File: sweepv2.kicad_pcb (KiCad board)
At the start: 2 copper layers, 216.9 x 86.9 mm, 51 parts, among them J1 AudioJack4dpb, J2 AudioJack4dpb, SW10 SW_Push, SW11 SW_Push, SW11_r1 SW_Push, SW12 SW_Push, SW12_r1 SW_Push, SW13_r1 SW_Push, SW14 SW_Push, SW15 SW_Push, SW15_r1 SW_Push, SW16 SW_Push, SW16_r1 SW_Push, SW17 SW_Push, SW17_r1 SW_Push, SW18 SW_Push, SW18_r1 SW_Push, SW2 SW_Push, SW20 SW_Push, SW20_r1 SW_Push, SW21 SW_Push, SW21_r1 SW_Push, SW2_r1 SW_Push, SW3 SW_Push, SW3_r1 SW_Push, SW4 SW_Push, SW4_r1 SW_Push, SW5 SW_Push, SW5_r1 SW_Push, SW6 SW_Push, SW6_r1 SW_Push, SW7_r1 SW_Push, SW8 SW_Push, SW8_r1 SW_Push, SW9 SW_Push, SW9_r1 SW_Push, U1 ProMicro-kbd, U2 ProMicro-kbd

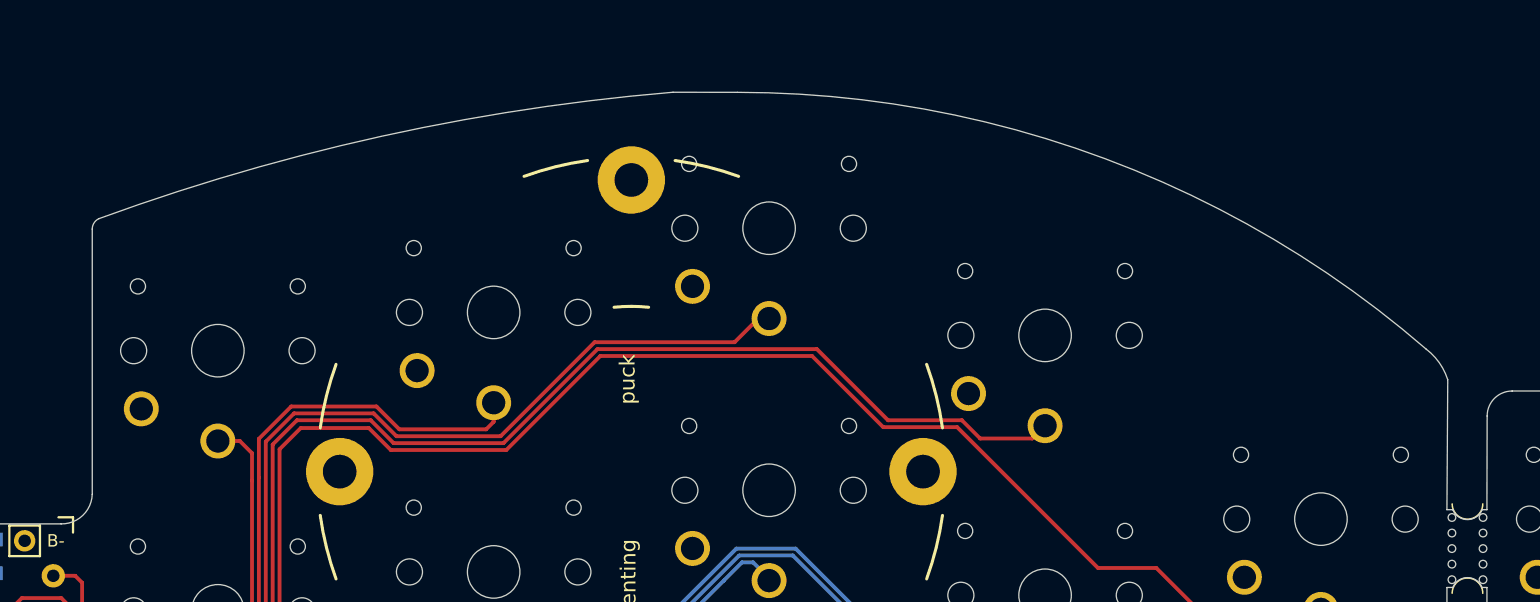
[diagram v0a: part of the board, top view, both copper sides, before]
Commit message: Copy cutout to other half
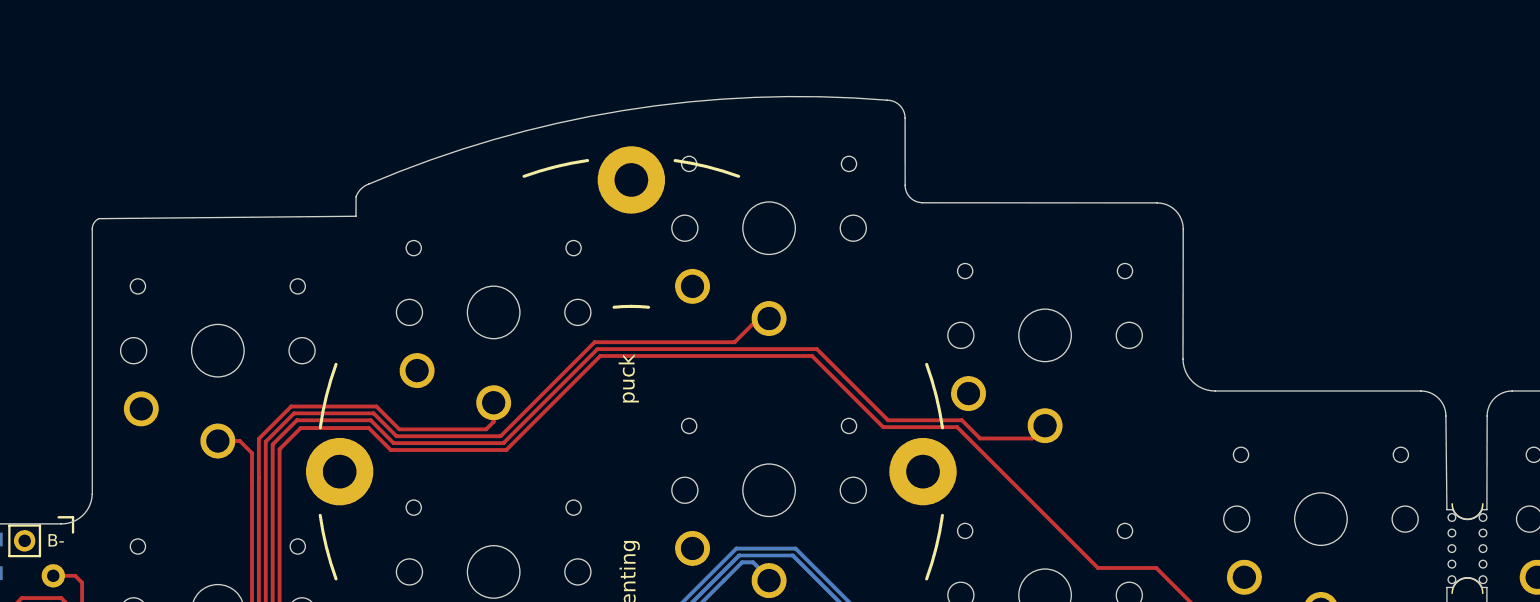
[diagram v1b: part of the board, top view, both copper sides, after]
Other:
- board size 216.9 x 86.9 mm -> 216.9 x 86.6 mm
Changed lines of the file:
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@@
   (gr_line (start 129.3495 77.724) (end 128.96 77.724) (layer "Edge.Cuts") (width 0.05))
   (gr_line (start 131.572 53.848) (end 131.572 72.644) (layer "Edge.Cuts") (width 0.05))
-  (gr_line (start 78.412223 21.502679) (end 82.613611 21.508139) (layer "Edge.Cuts") (width 0.05))
   (gr_line (start 21.792 50.442) (end 21.792 58.42) (layer "Edge.Cuts") (width 0.05))
   (gr_line (start 128.96 77.724) (end 128.975507 89.545022) (layer "Edge.Cuts") (width 0.05))
-  (gr_arc (start 127.587 38.265) (mid 128.457071 39.160882) (end 129.013945 40.278702) (layer "Edge.Cuts") (width 0.05))
   (gr_arc (start 128.975507 89.545022) (mid 128.324689 90.873432) (end 126.936 91.383119) (layer "Edge.Cuts") (width 0.05))
-  (gr_line (start 40.481999 47.763999) (end 40.481955 30.439419) (layer "Edge.Cuts") (width 0.05))
   (gr_line (start 21.792 66.548) (end 21.792 73.914) (layer "Edge.Cuts") (width 0.05))
   (gr_line (start 23.526696 88.85815) (end 34.034 107.451265) (layer "Edge.Cuts") (width 0.05))
   (gr_arc (start 40.481999 47.763999) (mid 39.859467 49.145717) (end 38.446998 49.694917) (layer "Edge.Cuts") (width 0.05))
-  (gr_arc (start 40.91671 29.758889) (mid 59.388121 24.375764) (end 78.412223 21.502679) (layer "Edge.Cuts") (width 0.05))
   (gr_arc (start 58.294866 98.863946) (mid 92.415558 93.289555) (end 126.936 91.383119) (layer "Edge.Cuts") (width 0.05))
   (gr_arc (start 23.526696 88.85815) (mid 22.237087 85.295347) (end 21.78 81.534) (layer "Edge.Cuts") (width 0.05))
@@
   (gr_line (start 38.446998 49.694917) (end 22.542 49.692) (layer "Edge.Cuts") (width 0.05))
   (gr_line (start 21.792 58.42) (end 21.792 66.548) (layer "Edge.Cuts") (width 0.05))
-  (gr_arc (start 40.481955 30.439419) (mid 40.599921 30.035645) (end 40.91671 29.758889) (layer "Edge.Cuts") (width 0.05))
   (gr_arc (start 36.766 108.05) (mid 35.275005 108.32098) (end 34.034 107.451265) (layer "Edge.Cuts") (width 0.05))
-  (gr_arc (start 82.613611 21.508139) (mid 106.610476 25.833455) (end 127.587 38.265) (layer "Edge.Cuts") (width 0.05))
   (gr_arc (start 36.766 108.05) (mid 47.217512 102.723597) (end 58.294866 98.863946) (layer "Edge.Cuts") (width 0.05))
   (gr_line (start 21.792 73.914) (end 21.78 81.534) (layer "Edge.Cuts") (width 0.05))
   (gr_line (start 128.96 53.848) (end 128.96 72.644) (layer "Edge.Cuts") (width 0.05))
-  (gr_line (start 129.013945 40.278702) (end 128.96 48.768) (layer "Edge.Cuts") (width 0.05))
+  (gr_arc (start 57.71268 28.330207) (mid 58.032549 27.821881) (end 58.540875 27.502012) (layer "Edge.Cuts") (width 0.05))
+  (gr_arc (start 58.540875 27.502012) (mid 75.136595 22.701228) (end 92.399358 22.021187) (layer "Edge.Cuts") (width 0.05))
+  (gr_line (start 93.56998 23.191809) (end 93.574586 27.576715) (layer "Edge.Cuts") (width 0.05))
+  (gr_arc (start 110.033903 28.730867) (mid 111.238908 29.229997) (end 111.738038 30.435002) (layer "Edge.Cuts") (width 0.05))
+  (gr_line (start 111.738038 30.435002) (end 111.721869 38.927938) (layer "Edge.Cuts") (width 0.05))
+  (gr_line (start 110.033903 28.730867) (end 94.708474 28.721612) (layer "Edge.Cuts") (width 0.05))
   (gr_line (start 133.216808 41.015954) (end 146.643428 41.015954) (layer "Edge.Cuts") (width 0.05))
+  (gr_line (start 113.836572 41.015954) (end 127.263192 41.015954) (layer "Edge.Cuts") (width 0.05))
   (gr_arc (start 201.939125 27.502012) (mid 202.447457 27.821875) (end 202.76732 28.330207) (layer "Edge.Cuts") (width 0.05))
   (gr_line (start 202.767321 28.330207) (end 202.770663 29.602302) (layer "Edge.Cuts") (width 0.05))
   (gr_arc (start 168.080642 22.021187) (mid 185.343405 22.701228) (end 201.939125 27.502012) (layer "Edge.Cuts") (width 0.05))
   (gr_line (start 131.572 48.768) (end 131.2545 48.768) (layer "Edge.Cuts") (width 0.05))
+  (gr_arc (start 127.263192 41.015954) (mid 128.415693 41.493335) (end 128.893074 42.645836) (layer "Edge.Cuts") (width 0.05))
+  (gr_arc (start 94.708474 28.71612) (mid 93.904741 28.38206) (end 93.574586 27.576715) (layer "Edge.Cuts") (width 0.05))
   (gr_line (start 148.758131 38.927938) (end 148.741962 30.435002) (layer "Edge.Cuts") (width 0.05))
   (gr_line (start 166.905414 27.576715) (end 166.91002 23.191809) (layer "Edge.Cuts") (width 0.05))
@@
   (gr_arc (start 131.254499 72.644) (mid 130.302 73.288873) (end 129.349501 72.643999) (layer "Edge.Cuts") (width 0.05))
   (gr_line (start 131.572 53.848) (end 131.2545 53.848) (layer "Edge.Cuts") (width 0.05))
+  (gr_arc (start 92.399358 22.021187) (mid 93.227113 22.364054) (end 93.56998 23.191809) (layer "Edge.Cuts") (width 0.05))
+  (gr_line (start 57.709337 29.602302) (end 40.91671 29.758889) (layer "Edge.Cuts") (width 0.05))
   (gr_arc (start 129.349501 77.724) (mid 130.302 77.079127) (end 131.254499 77.724001) (layer "Edge.Cuts") (width 0.05))
   (gr_arc (start 166.905414 27.576715) (mid 166.575259 28.38206) (end 165.771526 28.71612) (layer "Edge.Cuts") (width 0.05))
   (gr_arc (start 131.586926 42.645836) (mid 132.064307 41.493335) (end 133.216808 41.015954) (layer "Edge.Cuts") (width 0.05))
+  (gr_line (start 40.481955 30.439419) (end 40.481999 47.763999) (layer "Edge.Cuts") (width 0.05))
+  (gr_line (start 128.96 48.768) (end 128.893074 42.645836) (layer "Edge.Cuts") (width 0.05))
+  (gr_line (start 57.709337 29.602302) (end 57.712679 28.330207) (layer "Edge.Cuts") (width 0.05))
+  (gr_arc (start 40.481955 30.439419) (mid 40.599943 30.035659) (end 40.91671 29.758889) (layer "Edge.Cuts") (width 0.05))
   (gr_line (start 219.56329 29.758889) (end 202.770663 29.602302) (layer "Edge.Cuts") (width 0.05))
   (gr_arc (start 166.91002 23.191809) (mid 167.252887 22.364054) (end 168.080642 22.021187) (layer "Edge.Cuts") (width 0.05))
@@
   (gr_arc (start 129.349501 53.848) (mid 130.302 53.203127) (end 131.254499 53.848001) (layer "Edge.Cuts") (width 0.05))
   (gr_arc (start 148.741962 30.435002) (mid 149.241092 29.229997) (end 150.446097 28.730867) (layer "Edge.Cuts") (width 0.05))
+  (gr_arc (start 113.836572 41.015954) (mid 112.346856 40.409836) (end 111.721869 38.927938) (layer "Edge.Cuts") (width 0.05))
   (gr_text "Sweep v 2.2" (at 140.97 39.116) (layer "B.SilkS")
     (effects (font (size 1.5 1.5) (thickness 0.3)) (justify mirror))
@@
     )
   )
+  (group "" (id 4e900709-1a5b-403e-b36c-974add8b5403)
+    (members
+      00000000-0000-0000-0000-0000619805f5
+      00000000-0000-0000-0000-00006198060d
+      00000000-0000-0000-0000-0000619808c2
+      28bb64b5-d6a4-450b-b621-d35b54e55e63
+      31af7f7c-c0b8-419d-a577-eea91ca076f0
+      31e83ee7-f731-4f64-9bb8-31869d0560d6
+      34d0b0a2-263b-47e6-9437-576a7b894560
+      635fef95-0b63-4964-83a4-66e7c913fb9b
+      770c66e9-aab1-4df7-bad1-c38f3602d977
+      82c31248-9ca4-4633-85eb-bdcb6655e41b
+      97281869-2cc5-493b-9dac-524d21cf1503
+      98d02c4c-3e63-4812-9f8a-33e88dd28912
+      cfa37081-3abd-4b5e-b9bc-20330e9710eb
+      d20eb75f-71b1-4f57-a601-b4a8da2e62f4
+      dfacdfdb-8e52-4ffa-8465-efa73dc776c0
+      fcfb75f1-6bc9-4379-b1a5-eb8242f310ac
+    )
+  )

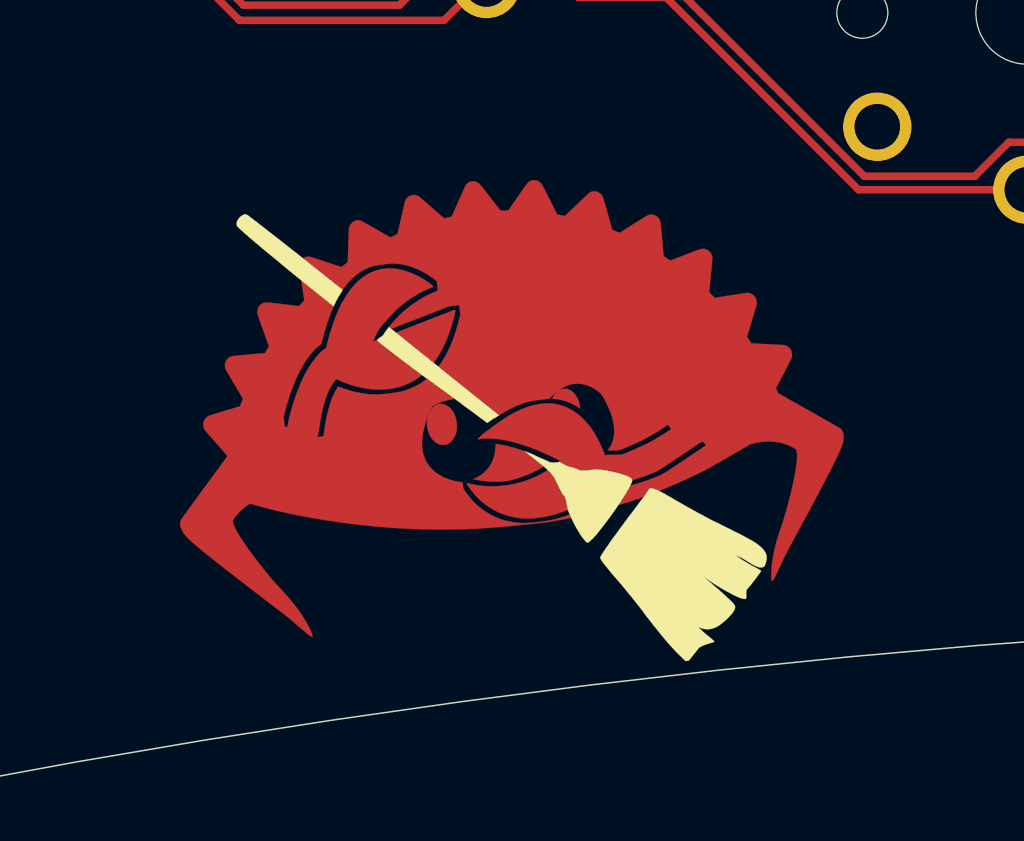
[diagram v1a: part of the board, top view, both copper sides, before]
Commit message: Remove sweep logo, refill shape
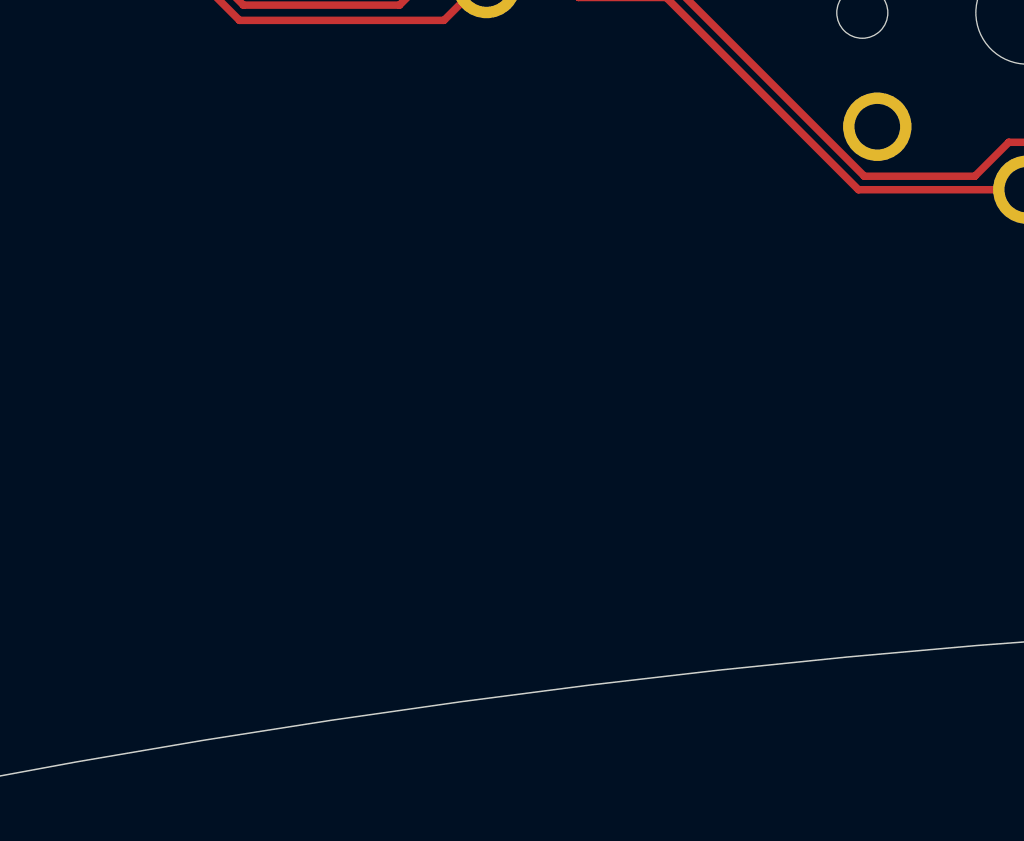
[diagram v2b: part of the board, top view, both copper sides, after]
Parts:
- removed G***: LOGO, Kailh:ferris_broom
